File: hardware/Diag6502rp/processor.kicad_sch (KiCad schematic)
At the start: 34 parts, among them J7 Conn_ARM_SWD_TagConnect_TC2030, SW1 SW_Push, U10 RP2350_80QFN, U9 W25Q128JVS, Y1 ABM8-272-T3

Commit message: Cleanup, Fiduciaries, component spacing
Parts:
- added FID1, FID2: Fiducial, Fiducial:Fiducial_1mm_Mask2mm, symbol Mechanical:Fiducial
- C16, C28: footprint Capacitor_SMD:C_0402_1005Metric_Pad0.74x0.62mm_HandSolder -> Capacitor_SMD:C_0402_1005Metric; LCSC Part # (none) -> C23733
- C17, C18, C19, C20, C21, C22, C23, C24, C25, C26, C27, C29: footprint Capacitor_SMD:C_0402_1005Metric_Pad0.74x0.62mm_HandSolder -> Capacitor_SMD:C_0402_1005Metric; LCSC Part # (none) -> C1525
- C30, C31: footprint Capacitor_SMD:C_0402_1005Metric_Pad0.74x0.62mm_HandSolder -> Capacitor_SMD:C_0402_1005Metric; LCSC Part # (none) -> C1548
- D3: LCSC Part # (none) -> C5355400
- R10, R12: footprint Resistor_SMD:R_0402_1005Metric_Pad0.72x0.64mm_HandSolder -> Resistor_SMD:R_0402_1005Metric; LCSC Part # (none) -> C25905
- R11, R13, R14: LCSC Part # (none) -> C25130
- R3: footprint Resistor_SMD:R_0402_1005Metric_Pad0.72x0.64mm_HandSolder -> Resistor_SMD:R_0402_1005Metric; LCSC Part # (none) -> C25077
- R4, R5: footprint Resistor_SMD:R_0402_1005Metric_Pad0.72x0.64mm_HandSolder -> Resistor_SMD:R_0402_1005Metric; LCSC Part # (none) -> C138021
- R6: footprint Resistor_SMD:R_0402_1005Metric_Pad0.72x0.64mm_HandSolder -> Resistor_SMD:R_0402_1005Metric; LCSC Part # (none) -> C25744
- R7, R8, R9: footprint Resistor_SMD:R_0402_1005Metric_Pad0.72x0.64mm_HandSolder -> Resistor_SMD:R_0402_1005Metric; LCSC Part # (none) -> C11702
- SW1: value SW_Push -> TS-1088-AR02016; footprint Button_Switch_SMD:SW_Push_1P1T_NO_CK_KMR2 -> footprints:TS-1088-xxxxxxx; LCSC Part # (none) -> C720477
- U10: LCSC Part # (none) -> C42415655
- U9: LCSC Part # (none) -> C97521
- Y1: LCSC Part # (none) -> C20625731

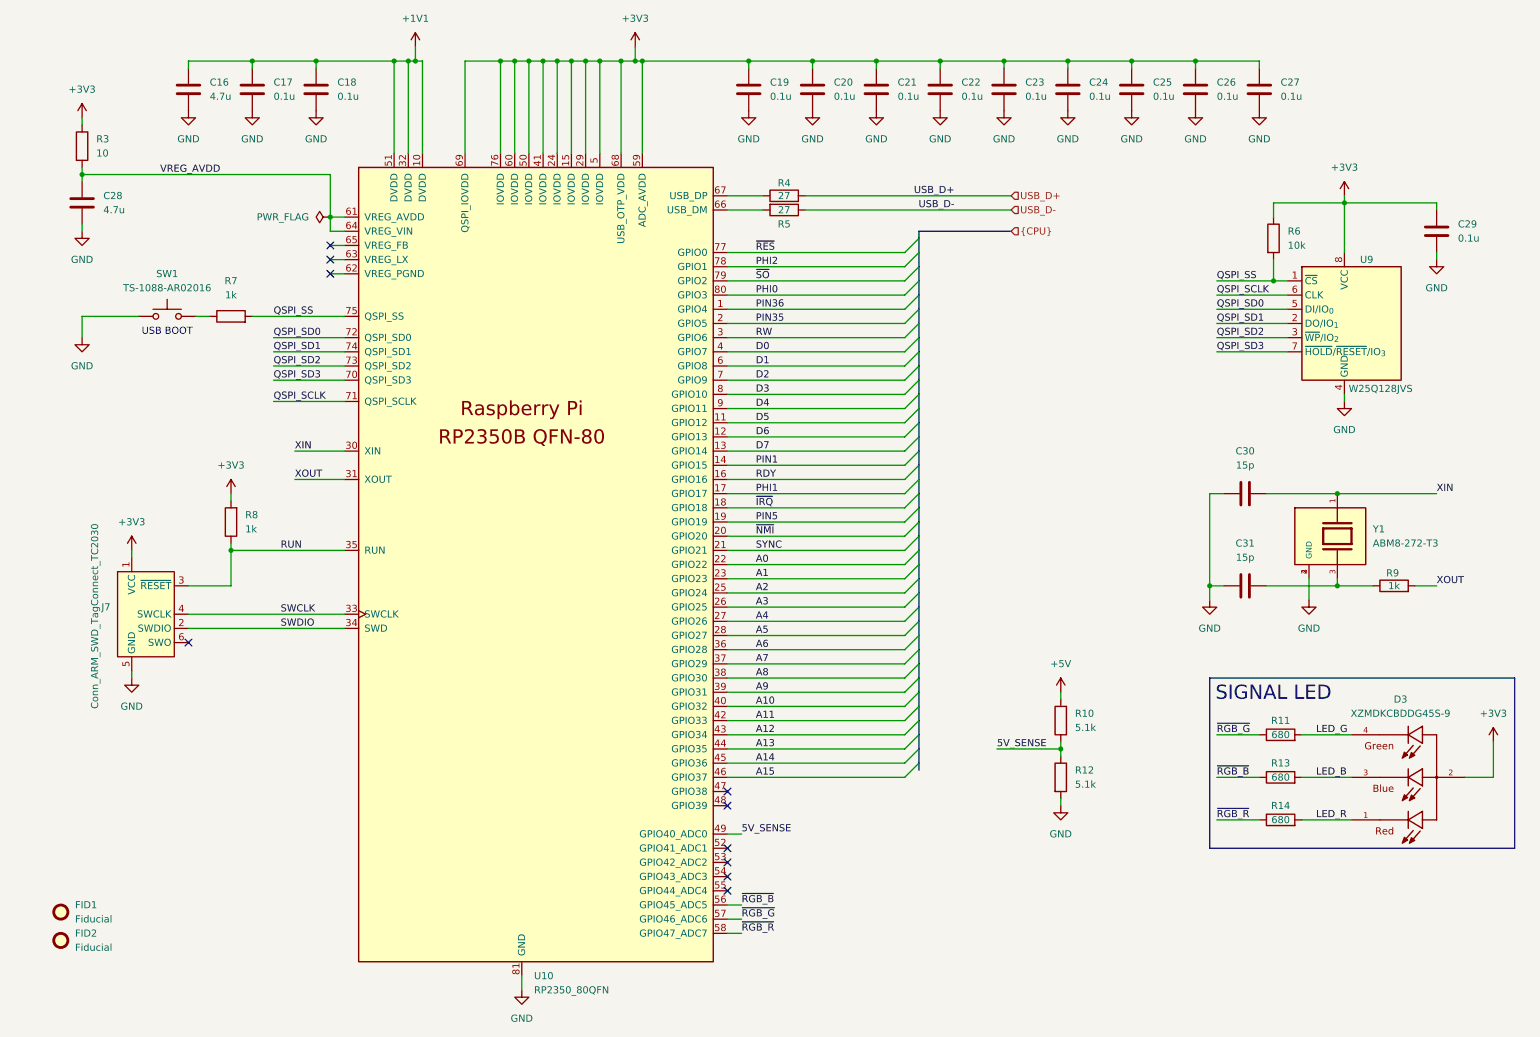
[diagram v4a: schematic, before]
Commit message: Added transfer and stitching vias.
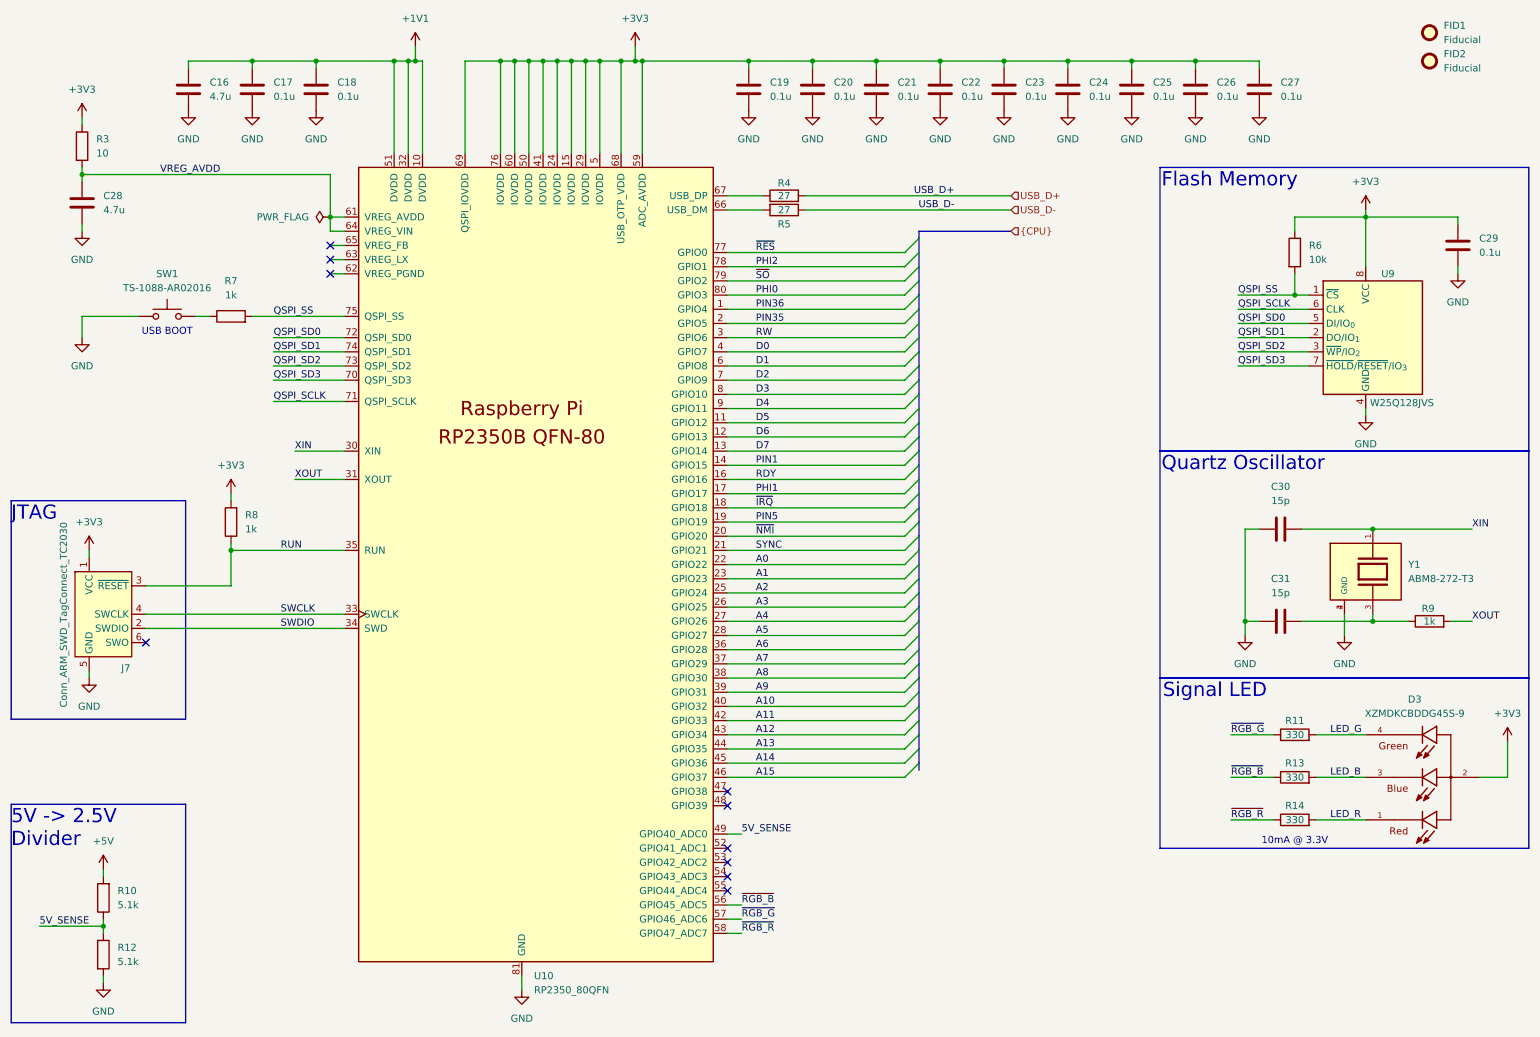
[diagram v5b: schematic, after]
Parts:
- R11, R13, R14: value 680 -> 330
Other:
- note added: "10mA @ 3.3V"
- note added: "5V -> 2.5V Divider"
- note added: "Flash Memory"
- note added: "JTAG"
- note added: "Quartz Oscillator"
- note added: "Signal LED"
- note removed: "SIGNAL LED"
- moved on the sheet: C29, C30, C31, D3, FID1, FID2, J7, R10, R11, R12, R13, R14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
